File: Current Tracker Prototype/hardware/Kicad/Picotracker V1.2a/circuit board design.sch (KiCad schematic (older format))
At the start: 30 parts, among them J1 Conn_01x10, J2 GND, J3 3.3V, J4 ICSS Logo, J5 Conn_01x01, Q1 IRLML6402, SW1 SW_Push, U1 MAX-M8C, U3 CMWX1ZZABZ-078, U6 MS5607-02BA

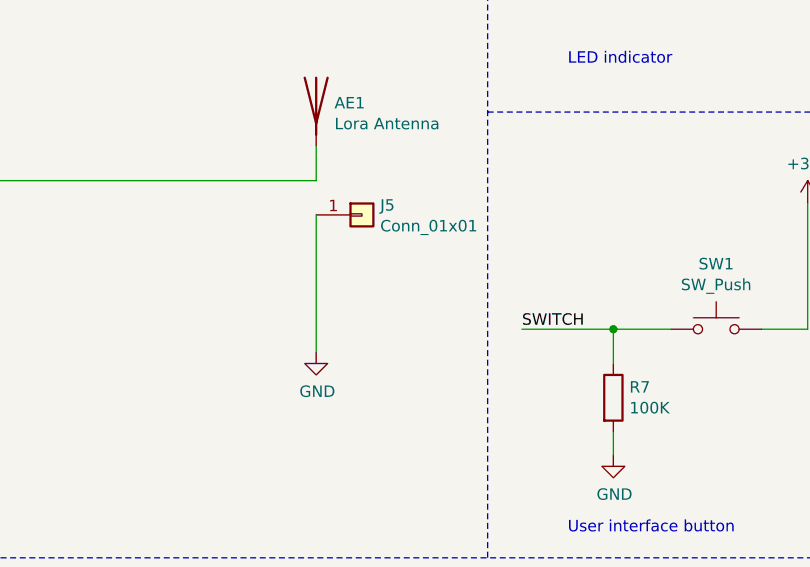
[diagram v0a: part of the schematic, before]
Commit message: put in the gnd hole for gnd plane. put in lots of vias
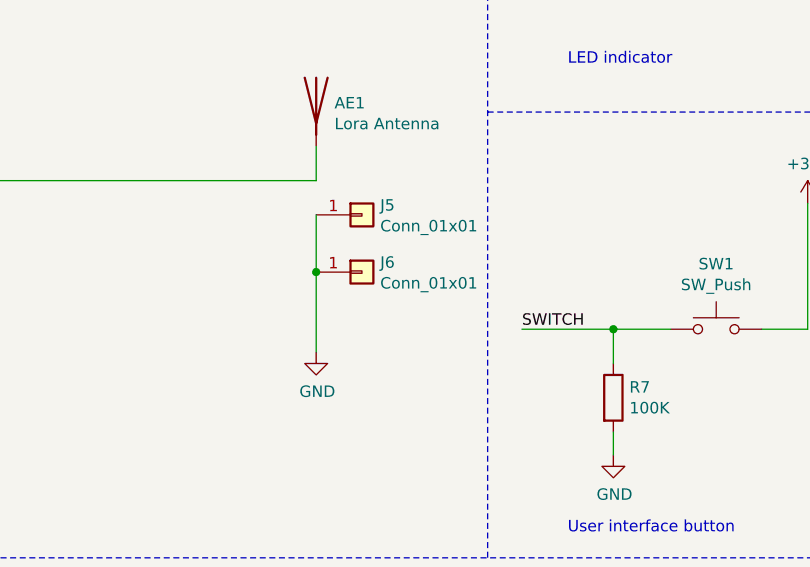
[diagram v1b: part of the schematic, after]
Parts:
- added J6: Conn_01x01, Connector_Wire:SolderWirePad_1x01_Drill0.8mm, symbol circuit-board-design-rescue:Conn_01x01-Connector_Generic
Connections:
- wire segments 134 -> 135
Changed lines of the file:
@@
 EESchema Schematic File Version 4
-EELAYER 30 0
+LIBS:circuit board design-cache
+EELAYER 29 0
 EELAYER END
 $Descr A3 16535 11693
@@
 $EndComp
 Wire Wire Line
-	8600 5350 8600 5950
+	8600 5350 8600 5600
 $Comp
 L circuit-board-design-rescue:R-Device R8
@@
 	1    0    0    1
 $EndComp
+$Comp
+L circuit-board-design-rescue:Conn_01x01-Connector_Generic J6
+U 1 1 5E3B5A9B
+P 8800 5600
+F 0 "J6" H 8880 5642 50  0000 L CNN
+F 1 "Conn_01x01" H 8880 5551 50  0000 L CNN
+F 2 "Connector_Wire:SolderWirePad_1x01_Drill0.8mm" H 8800 5600 50  0001 C CNN
+F 3 "~" H 8800 5600 50  0001 C CNN
+	1    8800 5600
+	1    0    0    -1
+$EndComp
+Connection ~ 8600 5600
+Wire Wire Line
+	8600 5600 8600 5950
 $EndSCHEMATC

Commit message: connect gps to usart2 port
pull gps ddc and uart pins out to side test points
connect stm32 reset line to vcc via resistor
connect stm32 to gps via usart2
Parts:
- removed C1: 100nF, Capacitor_SMD:C_0402_1005Metric, symbol circuit-board-design-rescue:C_Small-Device
- removed R7: 100K, Resistor_SMD:R_0402_1005Metric, symbol circuit-board-design-rescue:R-Device
- removed SW1: SW_Push, flight-computer:EVPAWCD4A, symbol circuit-board-design-rescue:SW_Push-Switch
- added R9: 10K, Resistor_SMD:R_0402_1005Metric, symbol circuit-board-design-rescue:R-Device
- added TP1, TP2, TP3, TP4: TestPoint, TestPoint:TestPoint_Pad_D2.0mm, symbol Connector:TestPoint
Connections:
- net labels added: USART2_RX, USART2_TX
- net labels removed: SWITCH
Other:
- note removed: "User interface button\n"

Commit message: put in the test points
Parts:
- added TP5, TP6, TP7, TP8: TestPoint, TestPoint:TestPoint_Pad_D1.0mm, symbol Connector:TestPoint
- TP1, TP2, TP3, TP4: footprint TestPoint:TestPoint_Pad_D2.0mm -> TestPoint:TestPoint_Pad_D1.0mm
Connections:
- wire segments 135 -> 143
- no-connect marks 31 -> 27

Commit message: put in test point to switched gps power supply
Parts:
- added svcc: TestPoint, TestPoint:TestPoint_Pad_D1.0mm, symbol Connector:TestPoint
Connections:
- wire segments 143 -> 146
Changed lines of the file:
@@
 Sheet 1 1
 Title "Pico lora tracker"
-Date "2019-11-27"
-Rev "1.1"
+Date "2020-08-19"
+Rev "1.3"
 Comp "Imperial College Space Society"
 Comment1 "Based on the Picotracker MK II and Project mach one flight computer"
@@
 Connection ~ 13150 6100
 Wire Wire Line
-	13350 6100 13350 6750
+	13350 6100 13350 6550
 Wire Wire Line
 	13350 6100 13150 6100
@@
 Wire Wire Line
 	8900 2600 8900 3300
+$Comp
+L Connector:TestPoint svcc
+U 1 1 5F57EBA2
+P 14000 6350
+F 0 "svcc" H 14058 6468 50  0000 L CNN
+F 1 "TestPoint" H 14050 6400 50  0000 L CNN
+F 2 "TestPoint:TestPoint_Pad_D1.0mm" H 14200 6350 50  0001 C CNN
+F 3 "~" H 14200 6350 50  0001 C CNN
+	1    14000 6350
+	1    0    0    -1
+$EndComp
+Wire Wire Line
+	13350 6550 14000 6550
+Wire Wire Line
+	14000 6550 14000 6350
+Connection ~ 13350 6550
+Wire Wire Line
+	13350 6550 13350 6750
 $EndSCHEMATC

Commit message: put test point name labels
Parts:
- renumbered svcc to TP9
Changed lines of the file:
@@
 	8900 2600 8900 3300
 $Comp
-L Connector:TestPoint svcc
+L Connector:TestPoint TP9
 U 1 1 5F57EBA2
 P 14000 6350
-F 0 "svcc" H 14058 6468 50  0000 L CNN
+F 0 "TP9" H 14058 6468 50  0000 L CNN
 F 1 "TestPoint" H 14050 6400 50  0000 L CNN
 F 2 "TestPoint:TestPoint_Pad_D1.0mm" H 14200 6350 50  0001 C CNN

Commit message: put in solder jumper for uart. Connected i2c as well
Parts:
- added JP1, JP2: SolderJumper_2_Open, Jumper:SolderJumper-2_P1.3mm_Open_RoundedPad1.0x1.5mm, symbol Jumper:SolderJumper_2_Open
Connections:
- wire segments 146 -> 148
- no-connect marks 27 -> 25
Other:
- moved on the sheet: C12, C13, Q1, R8, U1

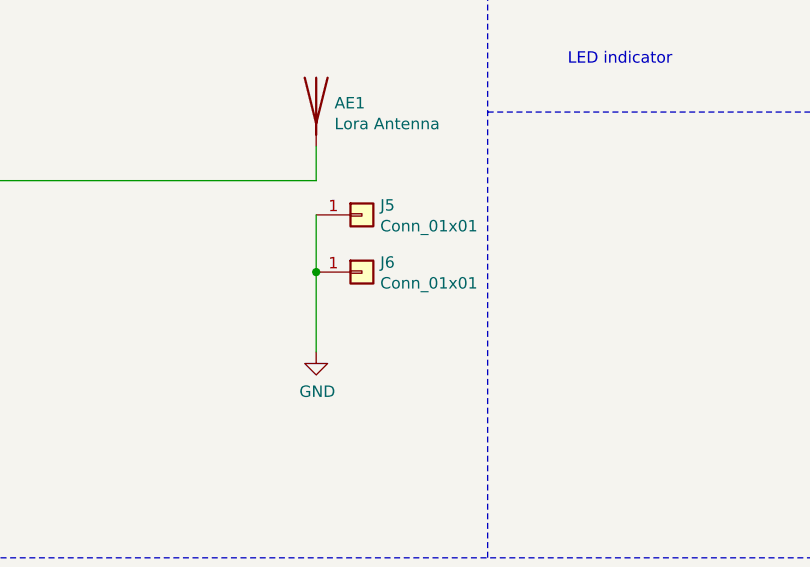
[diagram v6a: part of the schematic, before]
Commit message: changed the lora antenna pad to rectangular
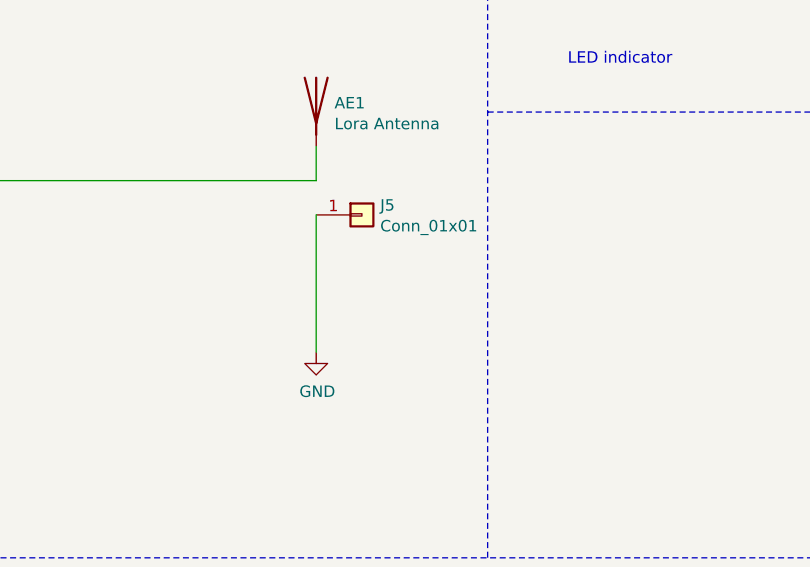
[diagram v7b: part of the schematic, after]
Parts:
- removed J6: Conn_01x01, Connector_Wire:SolderWirePad_1x01_Drill0.8mm, symbol circuit-board-design-rescue:Conn_01x01-Connector_Generic
- AE1: footprint Connector_Wire:SolderWirePad_1x01_Drill0.8mm -> pico_tracker:SolderWirePad_1x01_Drill0.8mm_square
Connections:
- wire segments 148 -> 147
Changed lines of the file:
@@
 F 0 "AE1" H 8680 4839 50  0000 L CNN
 F 1 "Lora Antenna" H 8680 4748 50  0000 L CNN
-F 2 "Connector_Wire:SolderWirePad_1x01_Drill0.8mm" H 8600 4850 50  0001 C CNN
+F 2 "pico_tracker:SolderWirePad_1x01_Drill0.8mm_square" H 8600 4850 50  0001 C CNN
 F 3 "~" H 8600 4850 50  0001 C CNN
 	1    8600 4850
@@
 	1    0    0    -1
 $EndComp
-Wire Wire Line
-	8600 5350 8600 5600
 $Comp
 L circuit-board-design-rescue:R-Device R8
@@
 	1    0    0    1
 $EndComp
-$Comp
-L circuit-board-design-rescue:Conn_01x01-Connector_Generic J6
-U 1 1 5E3B5A9B
-P 8800 5600
-F 0 "J6" H 8880 5642 50  0000 L CNN
-F 1 "Conn_01x01" H 8880 5551 50  0000 L CNN
-F 2 "Connector_Wire:SolderWirePad_1x01_Drill0.8mm" H 8800 5600 50  0001 C CNN
-F 3 "~" H 8800 5600 50  0001 C CNN
-	1    8800 5600
-	1    0    0    -1
-$EndComp
-Connection ~ 8600 5600
-Wire Wire Line
-	8600 5600 8600 5950
 Wire Wire Line
 	6450 2250 6750 2250
@@
 	1    0    0    -1
 $EndComp
+Wire Wire Line
+	8600 5350 8600 5950
 $EndSCHEMATC

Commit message: made seperate custom abz foot print
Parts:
- U3: footprint RF_Module:CMWX1ZZABZ -> pico_tracker:CMWX1ZZABZ_custom
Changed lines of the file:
@@
 F 0 "U3" H 5550 5500 50  0000 C CNN
 F 1 "CMWX1ZZABZ-078" H 5550 5350 50  0000 C CNN
-F 2 "RF_Module:CMWX1ZZABZ" H 6250 3900 50  0001 C CNN
+F 2 "pico_tracker:CMWX1ZZABZ_custom" H 6250 3900 50  0001 C CNN
 F 3 "https://wireless.murata.com/RFM/data/type_abz.pdf" H 8700 2400 50  0001 C CNN
 	1    6250 3900
